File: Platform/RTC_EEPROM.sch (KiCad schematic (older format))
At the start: 7 parts

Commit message: Added RTC and EEPROM
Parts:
- added BAT2: BS-7 3.3V, digikey-footprints:Battery_Holder_Coin_2032_BS-7, symbol dk_Battery-Holders-Clips-Contacts:BS-7
- added C10: 0.1U to 1UF, symbol Device:CP
- added R24, R25: 10K, symbol Device:R
- added R26, R27, R28, R29: 2K, symbol Device:R
- added U5: AT24CS32-SSHM, Package_SO:SOIC-8_3.9x4.9mm_P1.27mm, symbol Memory_EEPROM:AT24CS32-SSHM
- gave numbers to parts that had none: 7
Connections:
- net labels added: EEPROM, PA22, PA23, PA27, RTCC
- wire segments 28 -> 75
- no-connect marks 3 -> 2
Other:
- moved on the sheet: C9, R22, R23, U4

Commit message: changes
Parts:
- added TP1, TP2: TestPoint, symbol Connector:TestPoint
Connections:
- wire segments 75 -> 86
- no-connect marks 2 -> 0
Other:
- note added: "Reset pin is internally tied to High and \nrecommended not to use external pullup"
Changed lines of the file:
@@
 $EndComp
 $Comp
-L power:+3.3V #PWR0138
+L power:+3.3V #PWR042
 U 1 1 5FB0AC4A
 P 1700 2050
-F 0 "#PWR0138" H 1700 1900 50  0001 C CNN
+F 0 "#PWR042" H 1700 1900 50  0001 C CNN
 F 1 "+3.3V" H 1715 2223 50  0000 C CNN
 F 2 "" H 1700 2050 50  0001 C CNN
@@
 $EndComp
 $Comp
-L power:GND #PWR0139
+L power:GND #PWR043
 U 1 1 5FB0AFF3
 P 2950 3900
-F 0 "#PWR0139" H 2950 3650 50  0001 C CNN
+F 0 "#PWR043" H 2950 3650 50  0001 C CNN
 F 1 "GND" H 2955 3727 50  0000 C CNN
 F 2 "" H 2950 3900 50  0001 C CNN
@@
 	1450 2250 1700 2250
 Connection ~ 1700 2250
-NoConn ~ 3450 2700
-NoConn ~ 2450 3100
 $Comp
 L dk_Battery-Holders-Clips-Contacts:BS-7 BAT1
@@
 Connection ~ 1450 2250
 $Comp
-L power:GND #PWR0140
+L power:GND #PWR041
 U 1 1 5FB1839E
 P 950 2550
-F 0 "#PWR0140" H 950 2300 50  0001 C CNN
+F 0 "#PWR041" H 950 2300 50  0001 C CNN
 F 1 "GND" H 955 2377 50  0000 C CNN
 F 2 "" H 950 2550 50  0001 C CNN
@@
 F 0 "XTAL1" H 8900 2537 60  0000 C CNN
 F 1 "ECS-.327-6-17X-TR" H 8900 2431 60  0000 C CNN
-F 2 "XTAL_7X-TR_ECS" H 8900 2390 60  0001 C CNN
+F 2 "XTAL_7X-TR_ECS" H 8900 2390 60  0000 C CNN
 F 3 "" H 8100 2150 60  0000 C CNN
 	1    8100 2150
@@
 $EndComp
 Wire Wire Line
-	8100 2150 7450 2150
-Wire Wire Line
-	7450 2150 7450 2250
-Wire Wire Line
-	9700 2250 9700 2700
-Wire Wire Line
-	9700 2700 7450 2700
-Wire Wire Line
 	7450 2700 7450 2450
-$Comp
-L power:GND #PWR0141
-U 1 1 5FB2053E
-P 8100 2250
-F 0 "#PWR0141" H 8100 2000 50  0001 C CNN
-F 1 "GND" H 8105 2077 50  0000 C CNN
-F 2 "" H 8100 2250 50  0001 C CNN
-F 3 "" H 8100 2250 50  0001 C CNN
-	1    8100 2250
-	1    0    0    -1
-$EndComp
-$Comp
-L power:GND #PWR0142
-U 1 1 5FB20AAC
-P 9700 2150
-F 0 "#PWR0142" H 9700 1900 50  0001 C CNN
-F 1 "GND" V 9705 2022 50  0000 R CNN
-F 2 "" H 9700 2150 50  0001 C CNN
-F 3 "" H 9700 2150 50  0001 C CNN
-	1    9700 2150
-	0    -1   -1   0
-$EndComp
 $Comp
 L dk_Battery-Holders-Clips-Contacts:BS-7 BAT2
@@
 $EndComp
 $Comp
-L power:+3.3V #PWR0143
+L power:+3.3V #PWR049
 U 1 1 5FB41B68
 P 7050 1600
-F 0 "#PWR0143" H 7050 1450 50  0001 C CNN
+F 0 "#PWR049" H 7050 1450 50  0001 C CNN
 F 1 "+3.3V" H 7065 1773 50  0000 C CNN
 F 2 "" H 7050 1600 50  0001 C CNN
@@
 	7150 1950 7150 1450
 $Comp
-L power:GND #PWR0144
+L power:GND #PWR046
 U 1 1 5FB45206
 P 5350 1950
-F 0 "#PWR0144" H 5350 1700 50  0001 C CNN
+F 0 "#PWR046" H 5350 1700 50  0001 C CNN
 F 1 "GND" H 5355 1777 50  0000 C CNN
 F 2 "" H 5350 1950 50  0001 C CNN
@@
 $EndComp
 $Comp
-L power:GND #PWR0145
+L power:GND #PWR052
 U 1 1 5FB45567
-P 7500 1850
-F 0 "#PWR0145" H 7500 1600 50  0001 C CNN
-F 1 "GND" H 7505 1677 50  0000 C CNN
-F 2 "" H 7500 1850 50  0001 C CNN
-F 3 "" H 7500 1850 50  0001 C CNN
-	1    7500 1850
+P 7800 1850
+F 0 "#PWR052" H 7800 1600 50  0001 C CNN
+F 1 "GND" H 7805 1677 50  0000 C CNN
+F 2 "" H 7800 1850 50  0001 C CNN
+F 3 "" H 7800 1850 50  0001 C CNN
+	1    7800 1850
 	1    0    0    -1
 $EndComp
@@
 	5750 2250 5750 1950
 $Comp
-L power:GND #PWR0146
+L power:GND #PWR050
 U 1 1 5FB48AF2
 P 7050 3150
-F 0 "#PWR0146" H 7050 2900 50  0001 C CNN
+F 0 "#PWR050" H 7050 2900 50  0001 C CNN
 F 1 "GND" H 7055 2977 50  0000 C CNN
 F 2 "" H 7050 3150 50  0001 C CNN
@@
 	2950 3300 2950 3900
 $Comp
-L power:GND #PWR0147
+L power:GND #PWR045
 U 1 1 5FB4E0C4
-P 3950 2900
-F 0 "#PWR0147" H 3950 2650 50  0001 C CNN
-F 1 "GND" H 3955 2727 50  0000 C CNN
-F 2 "" H 3950 2900 50  0001 C CNN
-F 3 "" H 3950 2900 50  0001 C CNN
-	1    3950 2900
-	1    0    0    -1
-$EndComp
-Wire Wire Line
-	3950 2850 3950 2900
+P 4400 3000
+F 0 "#PWR045" H 4400 2750 50  0001 C CNN
+F 1 "GND" H 4405 2827 50  0000 C CNN
+F 2 "" H 4400 3000 50  0001 C CNN
+F 3 "" H 4400 3000 50  0001 C CNN
+	1    4400 3000
+	1    0    0    -1
+$EndComp
 $Comp
 L Device:R R24
@@
 $EndComp
 $Comp
-L power:+3.3V #PWR0148
+L power:+3.3V #PWR044
 U 1 1 5FB4F46E
 P 3600 2900
-F 0 "#PWR0148" H 3600 2750 50  0001 C CNN
+F 0 "#PWR044" H 3600 2750 50  0001 C CNN
 F 1 "+3.3V" H 3615 3073 50  0000 C CNN
 F 2 "" H 3600 2900 50  0001 C CNN
@@
 $EndComp
 $Comp
-L power:+3.3V #PWR0149
+L power:+3.3V #PWR047
 U 1 1 5FB52D8A
 P 6300 4550
-F 0 "#PWR0149" H 6300 4400 50  0001 C CNN
+F 0 "#PWR047" H 6300 4400 50  0001 C CNN
 F 1 "+3.3V" H 6315 4723 50  0000 C CNN
 F 2 "" H 6300 4550 50  0001 C CNN
@@
 	6300 4550 6300 4950
 $Comp
-L power:GND #PWR0150
+L power:GND #PWR048
 U 1 1 5FB53FDB
 P 6300 5750
-F 0 "#PWR0150" H 6300 5500 50  0001 C CNN
+F 0 "#PWR048" H 6300 5500 50  0001 C CNN
 F 1 "GND" H 6305 5577 50  0000 C CNN
 F 2 "" H 6300 5750 50  0001 C CNN
@@
 Wire Wire Line
 	2950 2250 3950 2250
+Wire Wire Line
+	7800 1850 7500 1850
+$Comp
+L power:GND #PWR051
+U 1 1 5FB575C0
+P 7750 2250
+F 0 "#PWR051" H 7750 2000 50  0001 C CNN
+F 1 "GND" H 7755 2077 50  0000 C CNN
+F 2 "" H 7750 2250 50  0001 C CNN
+F 3 "" H 7750 2250 50  0001 C CNN
+	1    7750 2250
+	1    0    0    -1
+$EndComp
+Wire Wire Line
+	7750 2250 8100 2250
+Wire Wire Line
+	9700 2250 9900 2250
+Wire Wire Line
+	9900 2250 9900 2700
+Wire Wire Line
+	7450 2700 9900 2700
+$Comp
+L power:GND #PWR053
+U 1 1 5FB5B09C
+P 10050 2300
+F 0 "#PWR053" H 10050 2050 50  0001 C CNN
+F 1 "GND" H 10055 2127 50  0000 C CNN
+F 2 "" H 10050 2300 50  0001 C CNN
+F 3 "" H 10050 2300 50  0001 C CNN
+	1    10050 2300
+	1    0    0    -1
+$EndComp
+Wire Wire Line
+	9700 2150 10050 2150
+Wire Wire Line
+	10050 2150 10050 2300
+Wire Wire Line
+	7450 2250 7600 2250
+Wire Wire Line
+	7600 2250 7600 2150
+Wire Wire Line
+	7600 2150 8100 2150
+Wire Wire Line
+	3950 2850 3950 3000
+Wire Wire Line
+	3950 3000 4400 3000
+Wire Notes Line
+	2500 3400 2500 4250
+Wire Notes Line
+	2500 4250 600  4250
+Wire Notes Line
+	600  4250 600  3400
+Wire Notes Line
+	600  3400 2500 3400
+Text Notes 800  3850 0    50   ~ 0
+Reset pin is internally tied to High and \nrecommended not to use external pullup
+$Comp
+L Connector:TestPoint TP1
+U 1 1 5FB718D1
+P 1800 3150
+F 0 "TP1" H 1858 3268 50  0000 L CNN
+F 1 "TestPoint" H 1858 3177 50  0000 L CNN
+F 2 "" H 2000 3150 50  0001 C CNN
+F 3 "~" H 2000 3150 50  0001 C CNN
+	1    1800 3150
+	1    0    0    -1
+$EndComp
+Wire Wire Line
+	1800 3150 2450 3150
+Wire Wire Line
+	2450 3150 2450 3100
+$Comp
+L Connector:TestPoint TP2
+U 1 1 5FB7652B
+P 3600 2550
+F 0 "TP2" H 3658 2668 50  0000 L CNN
+F 1 "TestPoint" H 3658 2577 50  0000 L CNN
+F 2 "" H 3800 2550 50  0001 C CNN
+F 3 "~" H 3800 2550 50  0001 C CNN
+	1    3600 2550
+	1    0    0    -1
+$EndComp
+Wire Wire Line
+	3600 2550 3600 2700
+Wire Wire Line
+	3600 2700 3450 2700
 $EndSCHEMATC

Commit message: Fixed ERC errors.
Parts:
- added R30, R31: 0E, symbol Device:R_Small
- BAT1, BAT2: symbol dk_Battery-Holders-Clips-Contacts:BS-7 -> Platform-rescue:BS-7-dk_Battery-Holders-Clips-Contacts
- XTAL1: symbol 2020-11-15_04-15-54:ECS-.327-6-17X-TR -> Platform-rescue:ECS-.327-6-17X-TR-2020-11-15_04-15-54
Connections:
- wire segments 86 -> 88
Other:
- note added: "added 0ohm resistors for easy rework."
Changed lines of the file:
@@
 Connection ~ 1700 2250
 $Comp
-L dk_Battery-Holders-Clips-Contacts:BS-7 BAT1
+L Platform-rescue:BS-7-dk_Battery-Holders-Clips-Contacts BAT1
 U 1 1 5FB1565A
 P 3950 2650
@@
 $EndComp
 $Comp
-L 2020-11-15_04-15-54:ECS-.327-6-17X-TR XTAL1
+L Platform-rescue:ECS-.327-6-17X-TR-2020-11-15_04-15-54 XTAL1
 U 1 1 5FB1EC3B
 P 8100 2150
+AR Path="/5FB1EC3B" Ref="XTAL1"  Part="1"
+AR Path="/5FB03683/5FB1EC3B" Ref="XTAL1"  Part="1"
 F 0 "XTAL1" H 8900 2537 60  0000 C CNN
 F 1 "ECS-.327-6-17X-TR" H 8900 2431 60  0000 C CNN
@@
 	7450 2700 7450 2450
 $Comp
-L dk_Battery-Holders-Clips-Contacts:BS-7 BAT2
+L Platform-rescue:BS-7-dk_Battery-Holders-Clips-Contacts BAT2
 U 1 1 5FB40A5C
 P 7500 1650
@@
 	7000 5150 6900 5150
 Connection ~ 6900 5150
-Text GLabel 1550 700  2    50   Input ~ 0
+Text GLabel 2050 700  2    50   Input ~ 0
 SDA
-Text GLabel 1550 900  2    50   Input ~ 0
+Text GLabel 2050 900  2    50   Input ~ 0
 SCL
 Text GLabel 1350 900  0    50   Input ~ 0
 PA23
-Wire Wire Line
-	1350 900  1550 900
 Text GLabel 1350 700  0    50   Input ~ 0
 PA22
-Wire Wire Line
-	1350 700  1550 700
 Wire Notes Line
 	550  600  3150 600
@@
 Wire Wire Line
 	3600 2700 3450 2700
+$Comp
+L Device:R_Small R30
+U 1 1 5FB9B802
+P 1700 700
+F 0 "R30" V 1650 600 50  0000 C CNN
+F 1 "0E" V 1750 700 50  0000 C CNN
+F 2 "" H 1700 700 50  0001 C CNN
+F 3 "~" H 1700 700 50  0001 C CNN
+	1    1700 700
+	0    1    1    0
+$EndComp
+$Comp
+L Device:R_Small R31
+U 1 1 5FB9BF59
+P 1700 900
+F 0 "R31" V 1650 800 50  0000 C CNN
+F 1 "0E" V 1800 900 50  0000 C CNN
+F 2 "" H 1700 900 50  0001 C CNN
+F 3 "~" H 1700 900 50  0001 C CNN
+	1    1700 900
+	0    1    1    0
+$EndComp
+Wire Wire Line
+	1350 900  1600 900
+Wire Wire Line
+	1800 900  2050 900
+Wire Wire Line
+	2050 700  1800 700
+Wire Wire Line
+	1600 700  1350 700
+Text Notes 950  1200 0    50   ~ 0
+added 0ohm resistors for easy rework.
 $EndSCHEMATC

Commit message: updated the crystal and cleared ERC errors.
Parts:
- removed BAT1: BS-7 3.3V, digikey-footprints:Battery_Holder_Coin_2032_BS-7, symbol Platform-rescue:BS-7-dk_Battery-Holders-Clips-Contacts
- removed XTAL1: ECS-.327-6-17X-TR, XTAL_7X-TR_ECS, symbol Platform-rescue:ECS-.327-6-17X-TR-2020-11-15_04-15-54
- added Y1: 32KHz crystal, symbol Device:Crystal_GND2
- renumbered BAT2 to BAT1
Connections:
- net labels added: VBAT
- wire segments 88 -> 87
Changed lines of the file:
@@
 Connection ~ 1700 2250
-$Comp
-L Platform-rescue:BS-7-dk_Battery-Holders-Clips-Contacts BAT1
-U 1 1 5FB1565A
-P 3950 2650
-F 0 "BAT1" H 4078 2703 60  0000 L CNN
-F 1 "BS-7    3.3V" H 4078 2597 60  0000 L CNN
-F 2 "digikey-footprints:Battery_Holder_Coin_2032_BS-7" H 4150 2850 60  0001 L CNN
-F 3 "http://www.memoryprotectiondevices.com/datasheets/BS-7-datasheet.pdf" V 4150 2950 60  0001 L CNN
-F 4 "BS-7-ND" H 4150 3050 60  0001 L CNN "Digi-Key_PN"
-F 5 "BS-7" H 4150 3150 60  0001 L CNN "MPN"
-F 6 "Battery Products" H 4150 3250 60  0001 L CNN "Category"
-F 7 "Battery Holders, Clips, Contacts" H 4150 3350 60  0001 L CNN "Family"
-F 8 "http://www.memoryprotectiondevices.com/datasheets/BS-7-datasheet.pdf" H 4150 3450 60  0001 L CNN "DK_Datasheet_Link"
-F 9 "/product-detail/en/mpd-memory-protection-devices/BS-7/BS-7-ND/389447" H 4150 3550 60  0001 L CNN "DK_Detail_Page"
-F 10 "BATTERY HOLDER COIN 20MM PC PIN" H 4150 3650 60  0001 L CNN "Description"
-F 11 "MPD (Memory Protection Devices)" H 4150 3750 60  0001 L CNN "Manufacturer"
-F 12 "Active" H 4150 3850 60  0001 L CNN "Status"
-	1    3950 2650
-	1    0    0    -1
-$EndComp
-Wire Wire Line
-	3950 2450 3950 2250
-Wire Wire Line
-	2950 2250 2950 2500
 $Comp
 L Device:CP C9
@@
 $EndComp
 $Comp
-L Platform-rescue:ECS-.327-6-17X-TR-2020-11-15_04-15-54 XTAL1
-U 1 1 5FB1EC3B
-P 8100 2150
-AR Path="/5FB1EC3B" Ref="XTAL1"  Part="1"
-AR Path="/5FB03683/5FB1EC3B" Ref="XTAL1"  Part="1"
-F 0 "XTAL1" H 8900 2537 60  0000 C CNN
-F 1 "ECS-.327-6-17X-TR" H 8900 2431 60  0000 C CNN
-F 2 "XTAL_7X-TR_ECS" H 8900 2390 60  0000 C CNN
-F 3 "" H 8100 2150 60  0000 C CNN
-	1    8100 2150
-	1    0    0    -1
-$EndComp
-Wire Wire Line
-	7450 2700 7450 2450
-$Comp
-L Platform-rescue:BS-7-dk_Battery-Holders-Clips-Contacts BAT2
+L Platform-rescue:BS-7-dk_Battery-Holders-Clips-Contacts BAT1
 U 1 1 5FB40A5C
 P 7500 1650
-F 0 "BAT2" H 7628 1703 60  0000 L CNN
+F 0 "BAT1" H 7628 1703 60  0000 L CNN
 F 1 "BS-7    3.3V" H 7628 1597 60  0000 L CNN
 F 2 "digikey-footprints:Battery_Holder_Coin_2032_BS-7" H 7700 1850 60  0001 L CNN
@@
 	2950 3300 2950 3900
 $Comp
-L power:GND #PWR045
-U 1 1 5FB4E0C4
-P 4400 3000
-F 0 "#PWR045" H 4400 2750 50  0001 C CNN
-F 1 "GND" H 4405 2827 50  0000 C CNN
-F 2 "" H 4400 3000 50  0001 C CNN
-F 3 "" H 4400 3000 50  0001 C CNN
-	1    4400 3000
-	1    0    0    -1
-$EndComp
-$Comp
 L Device:R R24
 U 1 1 5FB4ECAA
@@
 	7150 1450 7500 1450
 Wire Wire Line
-	2950 2250 3950 2250
-Wire Wire Line
 	7800 1850 7500 1850
-$Comp
-L power:GND #PWR051
-U 1 1 5FB575C0
-P 7750 2250
-F 0 "#PWR051" H 7750 2000 50  0001 C CNN
-F 1 "GND" H 7755 2077 50  0000 C CNN
-F 2 "" H 7750 2250 50  0001 C CNN
-F 3 "" H 7750 2250 50  0001 C CNN
-	1    7750 2250
-	1    0    0    -1
-$EndComp
-Wire Wire Line
-	7750 2250 8100 2250
-Wire Wire Line
-	9700 2250 9900 2250
-Wire Wire Line
-	9900 2250 9900 2700
-Wire Wire Line
-	7450 2700 9900 2700
-$Comp
-L power:GND #PWR053
-U 1 1 5FB5B09C
-P 10050 2300
-F 0 "#PWR053" H 10050 2050 50  0001 C CNN
-F 1 "GND" H 10055 2127 50  0000 C CNN
-F 2 "" H 10050 2300 50  0001 C CNN
-F 3 "" H 10050 2300 50  0001 C CNN
-	1    10050 2300
-	1    0    0    -1
-$EndComp
-Wire Wire Line
-	9700 2150 10050 2150
-Wire Wire Line
-	10050 2150 10050 2300
-Wire Wire Line
-	7450 2250 7600 2250
-Wire Wire Line
-	7600 2250 7600 2150
-Wire Wire Line
-	7600 2150 8100 2150
-Wire Wire Line
-	3950 2850 3950 3000
-Wire Wire Line
-	3950 3000 4400 3000
 Wire Notes Line
 	2500 3400 2500 4250
@@
 Text Notes 950  1200 0    50   ~ 0
 added 0ohm resistors for easy rework.
+$Comp
+L Device:Crystal_GND2 Y1
+U 1 1 5FBAC838
+P 7950 2350
+F 0 "Y1" V 7996 2481 50  0000 L CNN
+F 1 "32KHz crystal" V 8150 1750 50  0000 L CNN
+F 2 "" H 7950 2350 50  0001 C CNN
+F 3 "~" H 7950 2350 50  0001 C CNN
+	1    7950 2350
+	0    -1   -1   0
+$EndComp
+Wire Wire Line
+	7450 2250 7650 2250
+Wire Wire Line
+	7650 2250 7650 2100
+Wire Wire Line
+	7650 2100 7950 2100
+Wire Wire Line
+	7950 2100 7950 2200
+Wire Wire Line
+	7450 2450 7650 2450
+Wire Wire Line
+	7650 2450 7650 2600
+Wire Wire Line
+	7650 2600 7950 2600
+Wire Wire Line
+	7950 2600 7950 2500
+$Comp
+L power:GND #PWR051
+U 1 1 5FBB214B
+P 8250 2450
+F 0 "#PWR051" H 8250 2200 50  0001 C CNN
+F 1 "GND" H 8255 2277 50  0000 C CNN
+F 2 "" H 8250 2450 50  0001 C CNN
+F 3 "" H 8250 2450 50  0001 C CNN
+	1    8250 2450
+	1    0    0    -1
+$EndComp
+Wire Wire Line
+	8150 2350 8250 2350
+Wire Wire Line
+	8250 2350 8250 2450
+Text GLabel 7600 1300 2    50   Output ~ 0
+VBAT
+Wire Wire Line
+	7600 1300 7500 1300
+Wire Wire Line
+	7500 1300 7500 1450
+Connection ~ 7500 1450
+Text GLabel 3050 2250 2    50   Input ~ 0
+VBAT
+Wire Wire Line
+	3050 2250 2950 2250
+Wire Wire Line
+	2950 2250 2950 2500
 $EndSCHEMATC

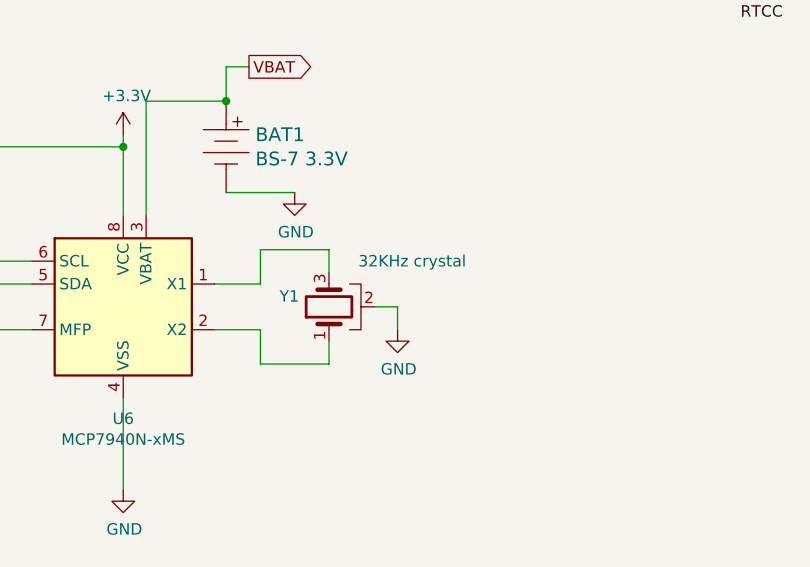
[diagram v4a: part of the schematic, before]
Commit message: added caps for the crystal.
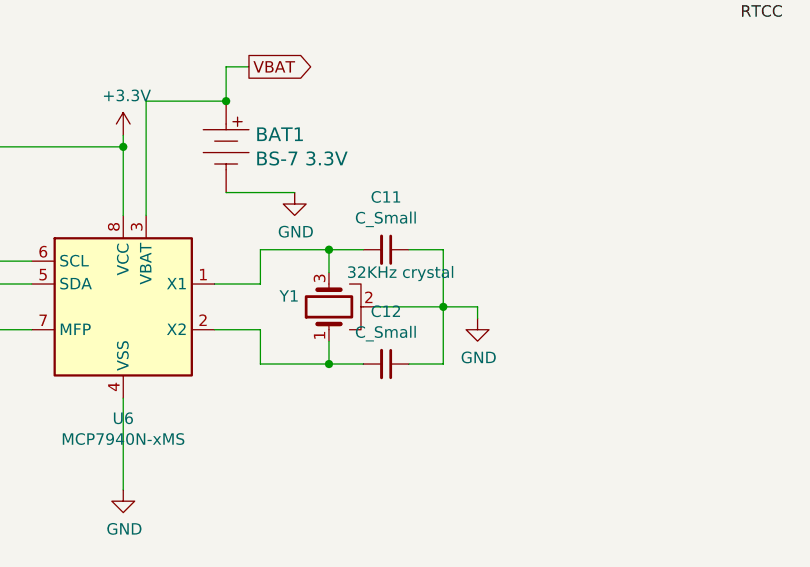
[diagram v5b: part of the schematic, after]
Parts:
- added C11, C12: C_Small, symbol Device:C_Small
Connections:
- net GND: now also C11.1, C12.1
- net at U6.1 (X1), Y1.3: now also C11.2
- net at U6.2 (X2), Y1.1: now also C12.2
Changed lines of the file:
@@
 P 7950 2350
 F 0 "Y1" V 7996 2481 50  0000 L CNN
-F 1 "32KHz crystal" V 8150 1750 50  0000 L CNN
+F 1 "32KHz crystal" V 8100 1800 50  0000 L CNN
 F 2 "" H 7950 2350 50  0001 C CNN
 F 3 "~" H 7950 2350 50  0001 C CNN
@@
 L power:GND #PWR051
 U 1 1 5FBB214B
-P 8250 2450
-F 0 "#PWR051" H 8250 2200 50  0001 C CNN
-F 1 "GND" H 8255 2277 50  0000 C CNN
-F 2 "" H 8250 2450 50  0001 C CNN
-F 3 "" H 8250 2450 50  0001 C CNN
-	1    8250 2450
+P 8600 2400
+F 0 "#PWR051" H 8600 2150 50  0001 C CNN
+F 1 "GND" H 8605 2227 50  0000 C CNN
+F 2 "" H 8600 2400 50  0001 C CNN
+F 3 "" H 8600 2400 50  0001 C CNN
+	1    8600 2400
 	1    0    0    -1
 $EndComp
-Wire Wire Line
-	8150 2350 8250 2350
-Wire Wire Line
-	8250 2350 8250 2450
 Text GLabel 7600 1300 2    50   Output ~ 0
 VBAT
@@
 Wire Wire Line
 	2950 2250 2950 2500
+$Comp
+L Device:C_Small C11
+U 1 1 5FBA201D
+P 8200 2100
+F 0 "C11" V 7971 2100 50  0000 C CNN
+F 1 "C_Small" V 8062 2100 50  0000 C CNN
+F 2 "" H 8200 2100 50  0001 C CNN
+F 3 "~" H 8200 2100 50  0001 C CNN
+	1    8200 2100
+	0    1    1    0
+$EndComp
+$Comp
+L Device:C_Small C12
+U 1 1 5FBA2B99
+P 8200 2600
+F 0 "C12" V 7971 2600 50  0000 C CNN
+F 1 "C_Small" V 8062 2600 50  0000 C CNN
+F 2 "" H 8200 2600 50  0001 C CNN
+F 3 "~" H 8200 2600 50  0001 C CNN
+	1    8200 2600
+	0    1    1    0
+$EndComp
+Wire Wire Line
+	8100 2100 7950 2100
+Connection ~ 7950 2100
+Wire Wire Line
+	7950 2600 8100 2600
+Connection ~ 7950 2600
+Wire Wire Line
+	8300 2100 8450 2100
+Wire Wire Line
+	8450 2100 8450 2350
+Wire Wire Line
+	8450 2600 8300 2600
+Wire Wire Line
+	8450 2350 8600 2350
+Wire Wire Line
+	8600 2350 8600 2400
+Connection ~ 8450 2350
+Wire Wire Line
+	8450 2350 8450 2600
+Wire Wire Line
+	8150 2350 8450 2350
 $EndSCHEMATC

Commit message: updated.
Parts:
- BAT1: symbol Platform-rescue:BS-7-dk_Battery-Holders-Clips-Contacts -> Platform-rescue:BS-7-dk_Battery-Holders-Clips-Contacts-Platform-rescue
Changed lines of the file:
@@
 $EndComp
 $Comp
-L Platform-rescue:BS-7-dk_Battery-Holders-Clips-Contacts BAT1
+L Platform-rescue:BS-7-dk_Battery-Holders-Clips-Contacts-Platform-rescue BAT1
 U 1 1 5FB40A5C
 P 7500 1650
